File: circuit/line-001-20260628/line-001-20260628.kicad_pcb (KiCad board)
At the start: 2 copper layers, 163.1 x 133.7 mm, 226 parts, among them J1 Conn_01x02_Pin, J2 Conn_01x02_Pin, J3 ICSP, J4 USB_C_Receptacle_USB2.0_16P, Q1 Q_Photo_NPN_CE, Q10 Q_Photo_NPN_CE, Q11 Q_Photo_NPN_CE, Q12 Q_Photo_NPN_CE, Q13 Q_Photo_NPN_CE, Q14 Q_Photo_NPN_CE, Q15 Q_Photo_NPN_CE, Q16 Q_Photo_NPN_CE, Q17 Q_Photo_NPN_CE, Q18 Q_Photo_NPN_CE, Q19 Q_Photo_NPN_CE, Q2 Q_Photo_NPN_CE, Q20 Q_Photo_NPN_CE, Q21 Q_Photo_NPN_CE, Q22 Q_Photo_NPN_CE, Q23 Q_Photo_NPN_CE, Q24 Q_Photo_NPN_CE, Q25 Q_Photo_NPN_CE, Q26 Q_Photo_NPN_CE, Q27 Q_Photo_NPN_CE, Q28 Q_Photo_NPN_CE, Q29 Q_Photo_NPN_CE, Q3 Q_Photo_NPN_CE, Q30 Q_Photo_NPN_CE, Q31 Q_Photo_NPN_CE, Q32 Q_Photo_NPN_CE, Q37 Q_Photo_NPN_CE, Q38 Q_Photo_NPN_CE, Q39 Q_Photo_NPN_CE, Q4 Q_Photo_NPN_CE, Q40 Q_Photo_NPN_CE, Q5 Q_Photo_NPN_CE, Q6 Q_Photo_NPN_CE, Q7 Q_Photo_NPN_CE, Q8 Q_Photo_NPN_CE, Q9 Q_Photo_NPN_CE, SW1 SW_Push, SW2 SW_SPDT, U1 LM393DR, U10 LM393DR, U11 LM393DR, U12 LM393DR, U13 LM393DR, U14 LM393DR, U15 LM393DR, U16 LM393DR, U17 ATmega2560-16A, U18 CH340G, U2 LM393DR, U3 LM393DR, U4 LM393DR, U5 LM393DR, U6 LM393DR, U7 LM393DR, U8 LM393DR, U9 LM393DR, Y1 16MHz, Y2 12MHz

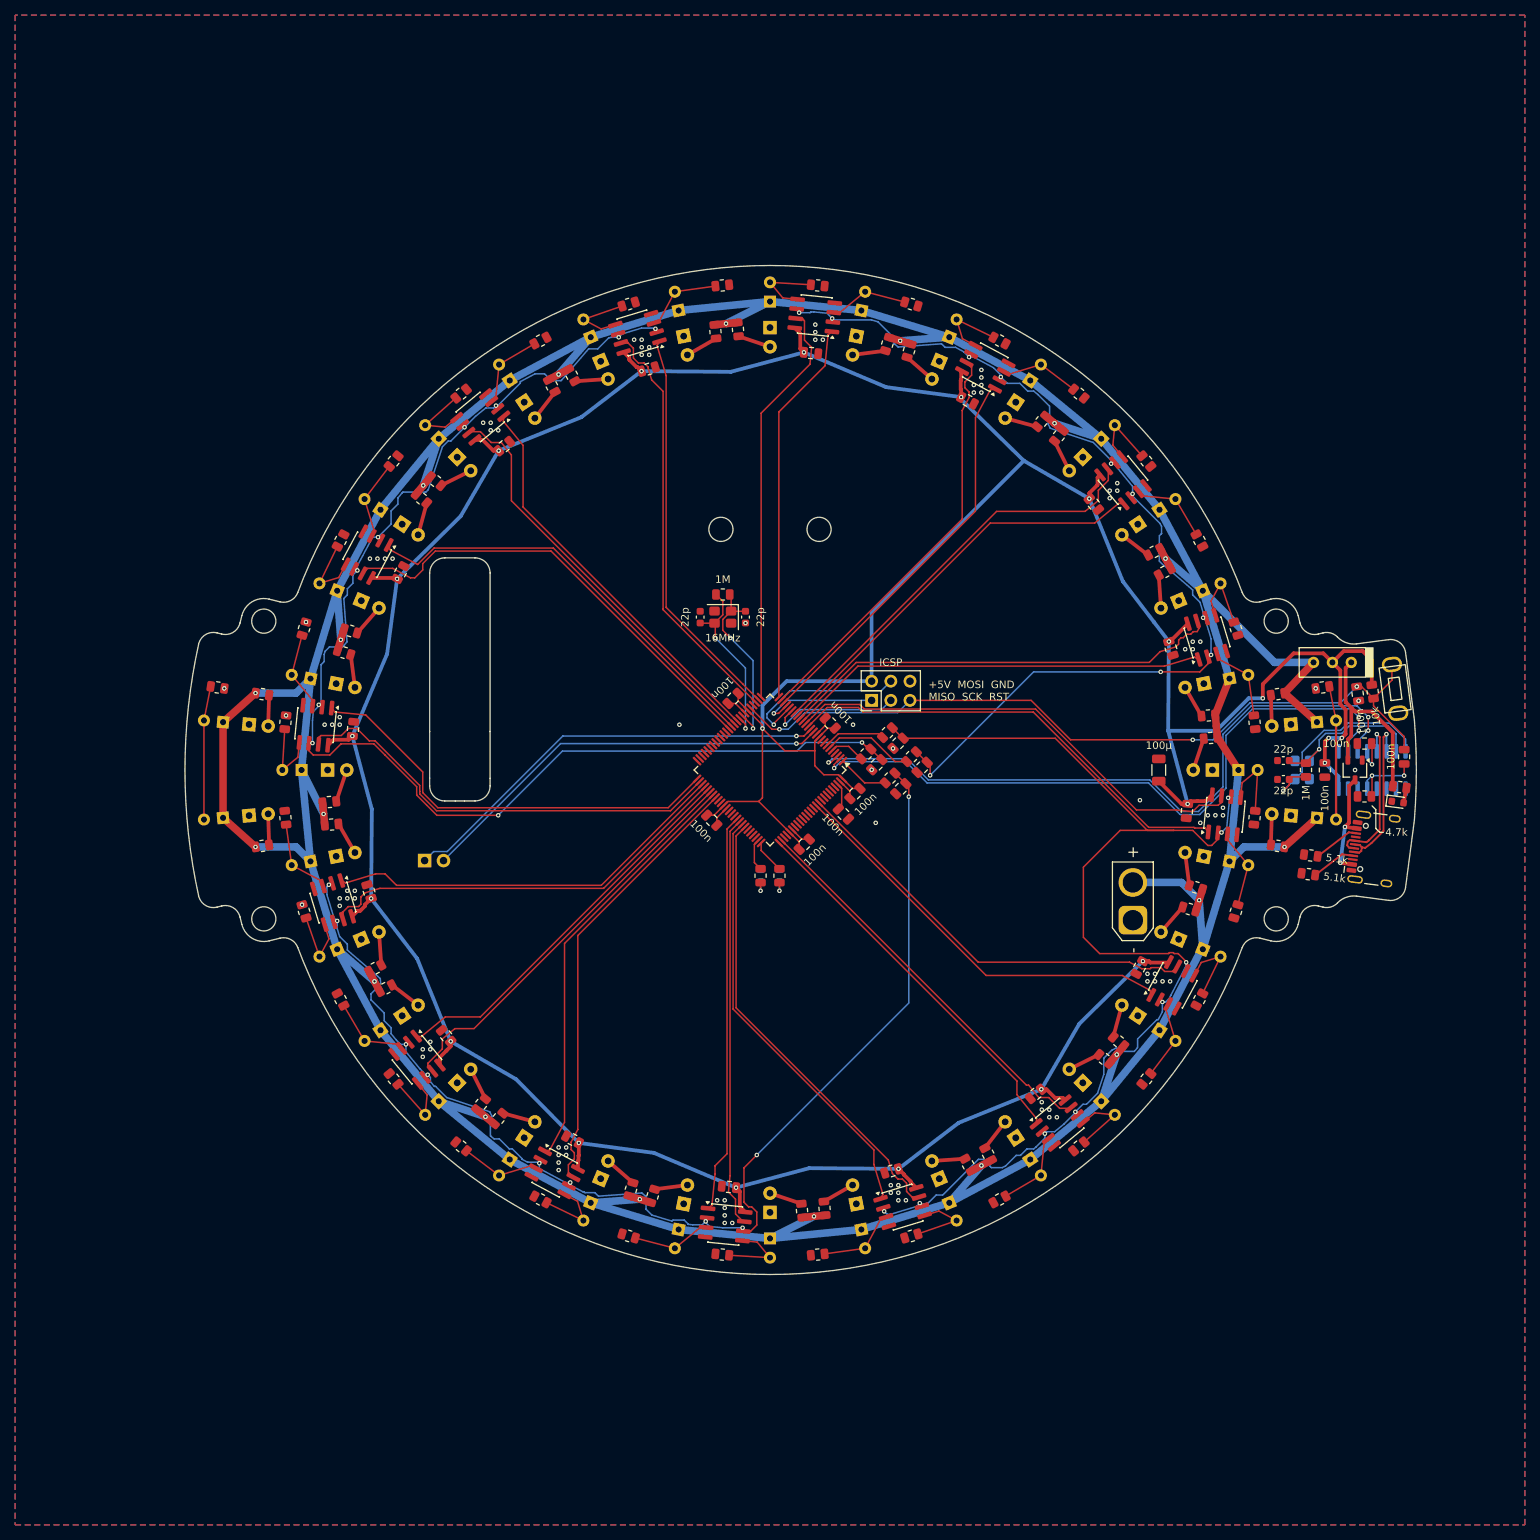
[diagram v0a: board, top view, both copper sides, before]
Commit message: Update ラインセンサ基板にGNDビアを打った
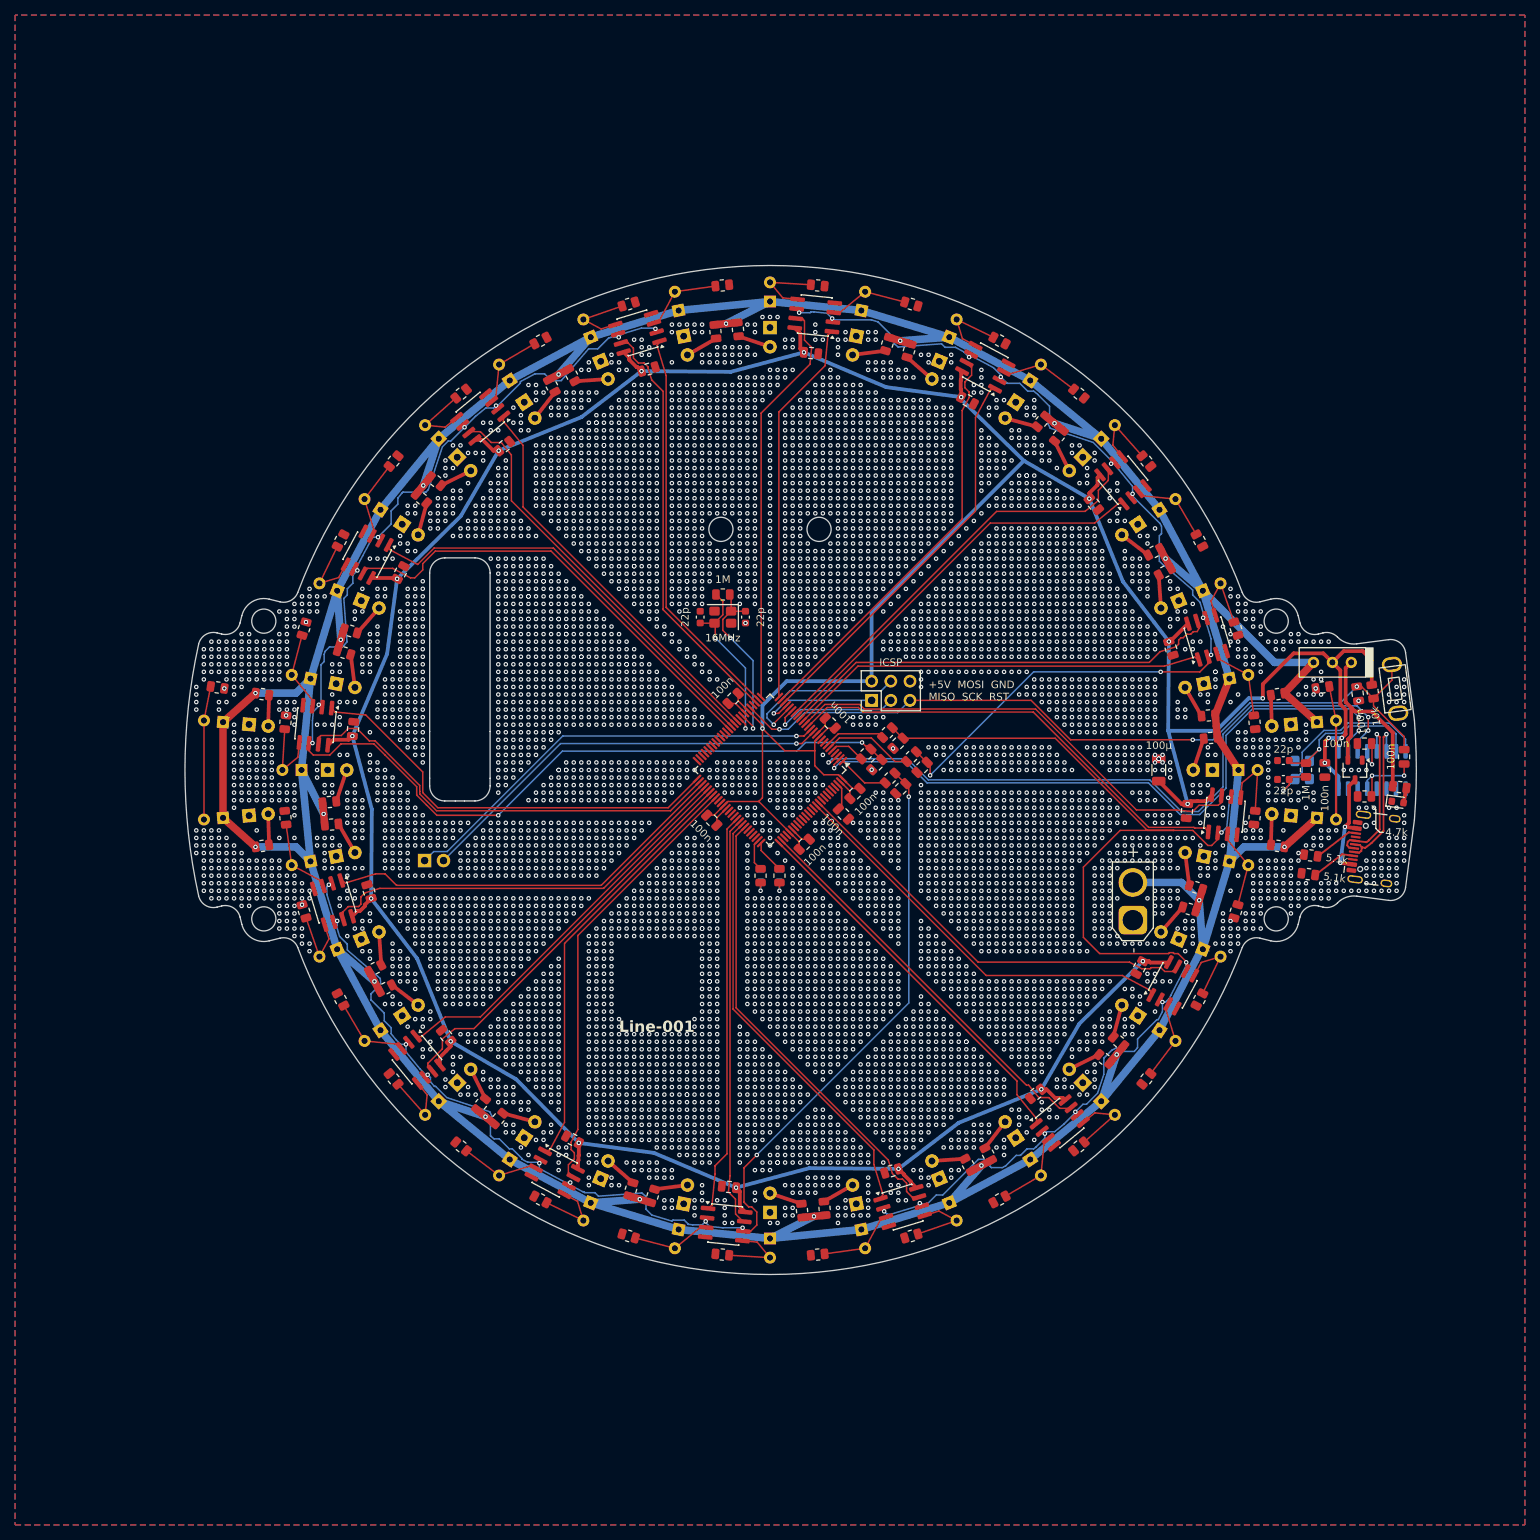
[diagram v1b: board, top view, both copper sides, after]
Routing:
- net GND: vias 94 -> 7149
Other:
- board text added: "Line-001"

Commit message: Update ラインセンサ基板の回路図とボード図を更新
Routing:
- net GND: vias 7149 -> 6489
